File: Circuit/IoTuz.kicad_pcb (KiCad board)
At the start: 2 copper layers, 150 x 95 mm, 93 parts, among them J1 Jack.3.5mm-Mono, P1 ALLIGATOR_01X35, P2 BATTERY, P3 USB_5PIN_SHELL, P4 LED_1, P5 LED_2, P8 IRReceiver, Q1 S8050, Q2 S8050, Q202 FDN340P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

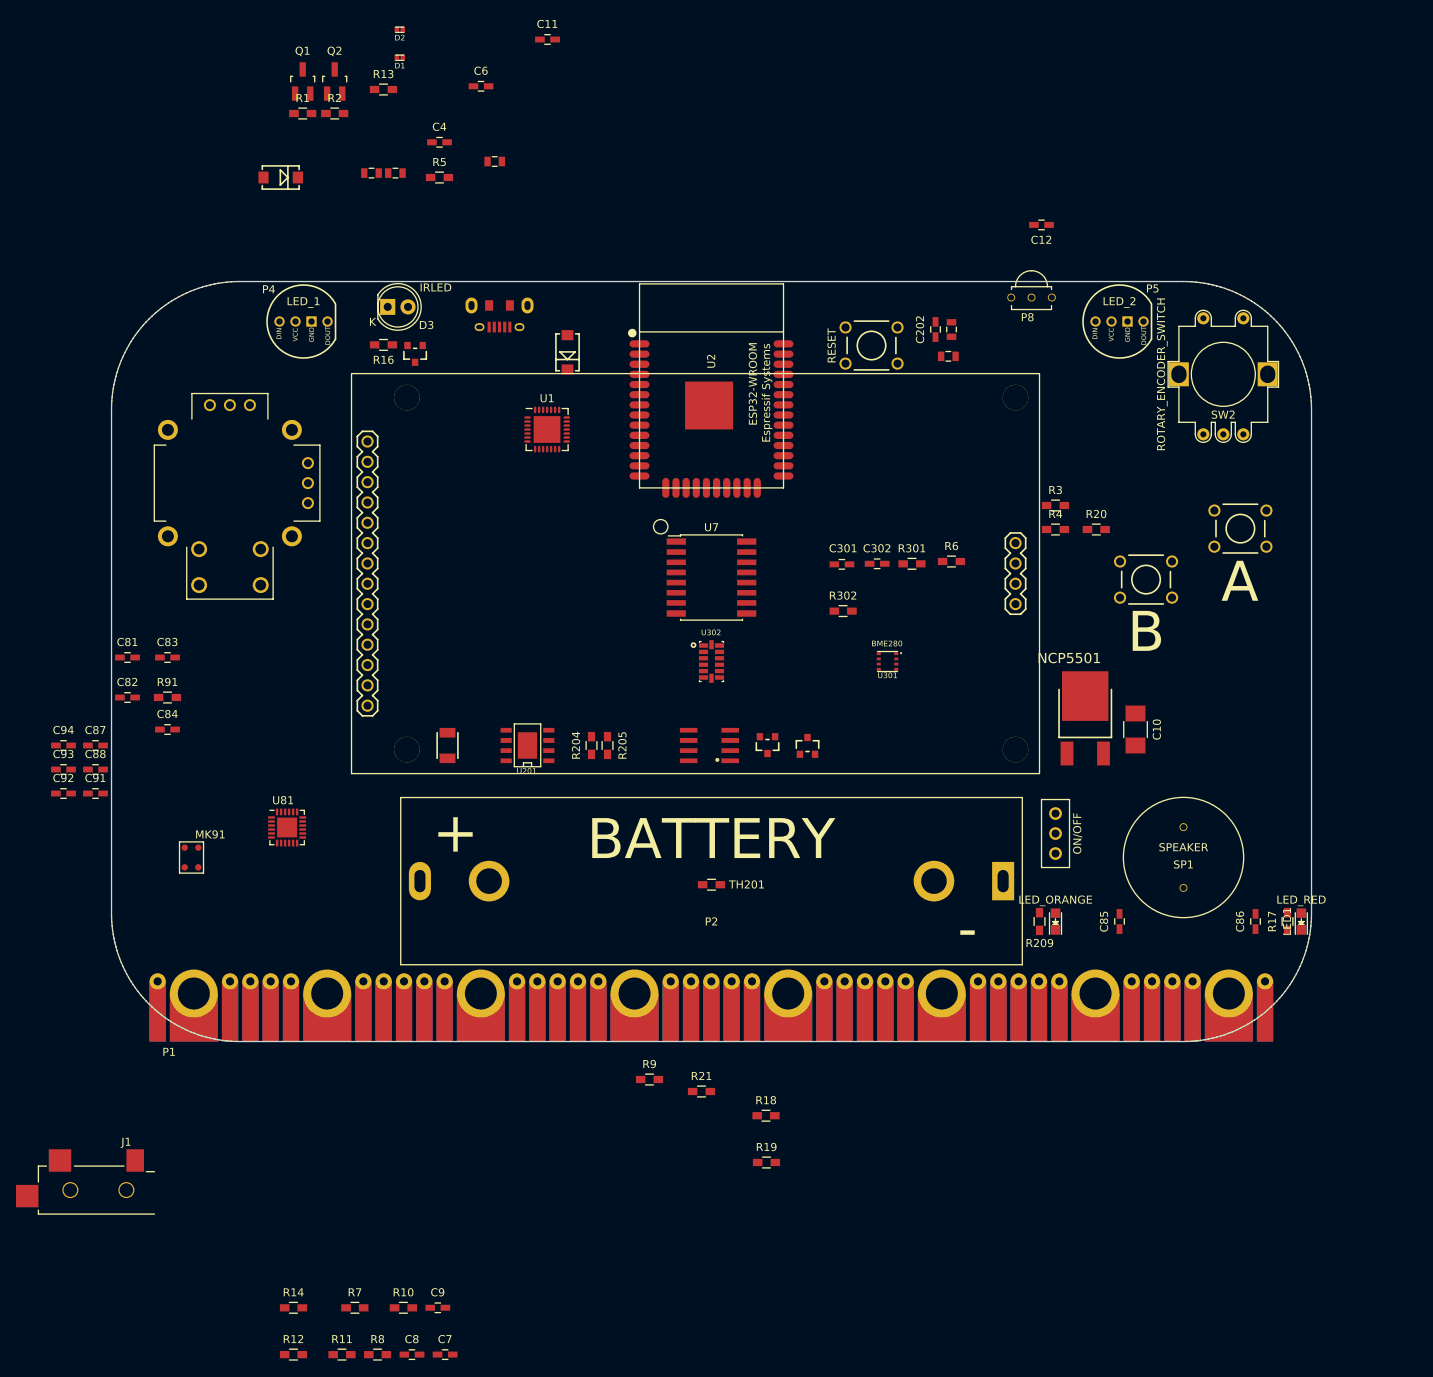
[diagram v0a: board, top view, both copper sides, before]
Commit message: Sectioning nearly complete.
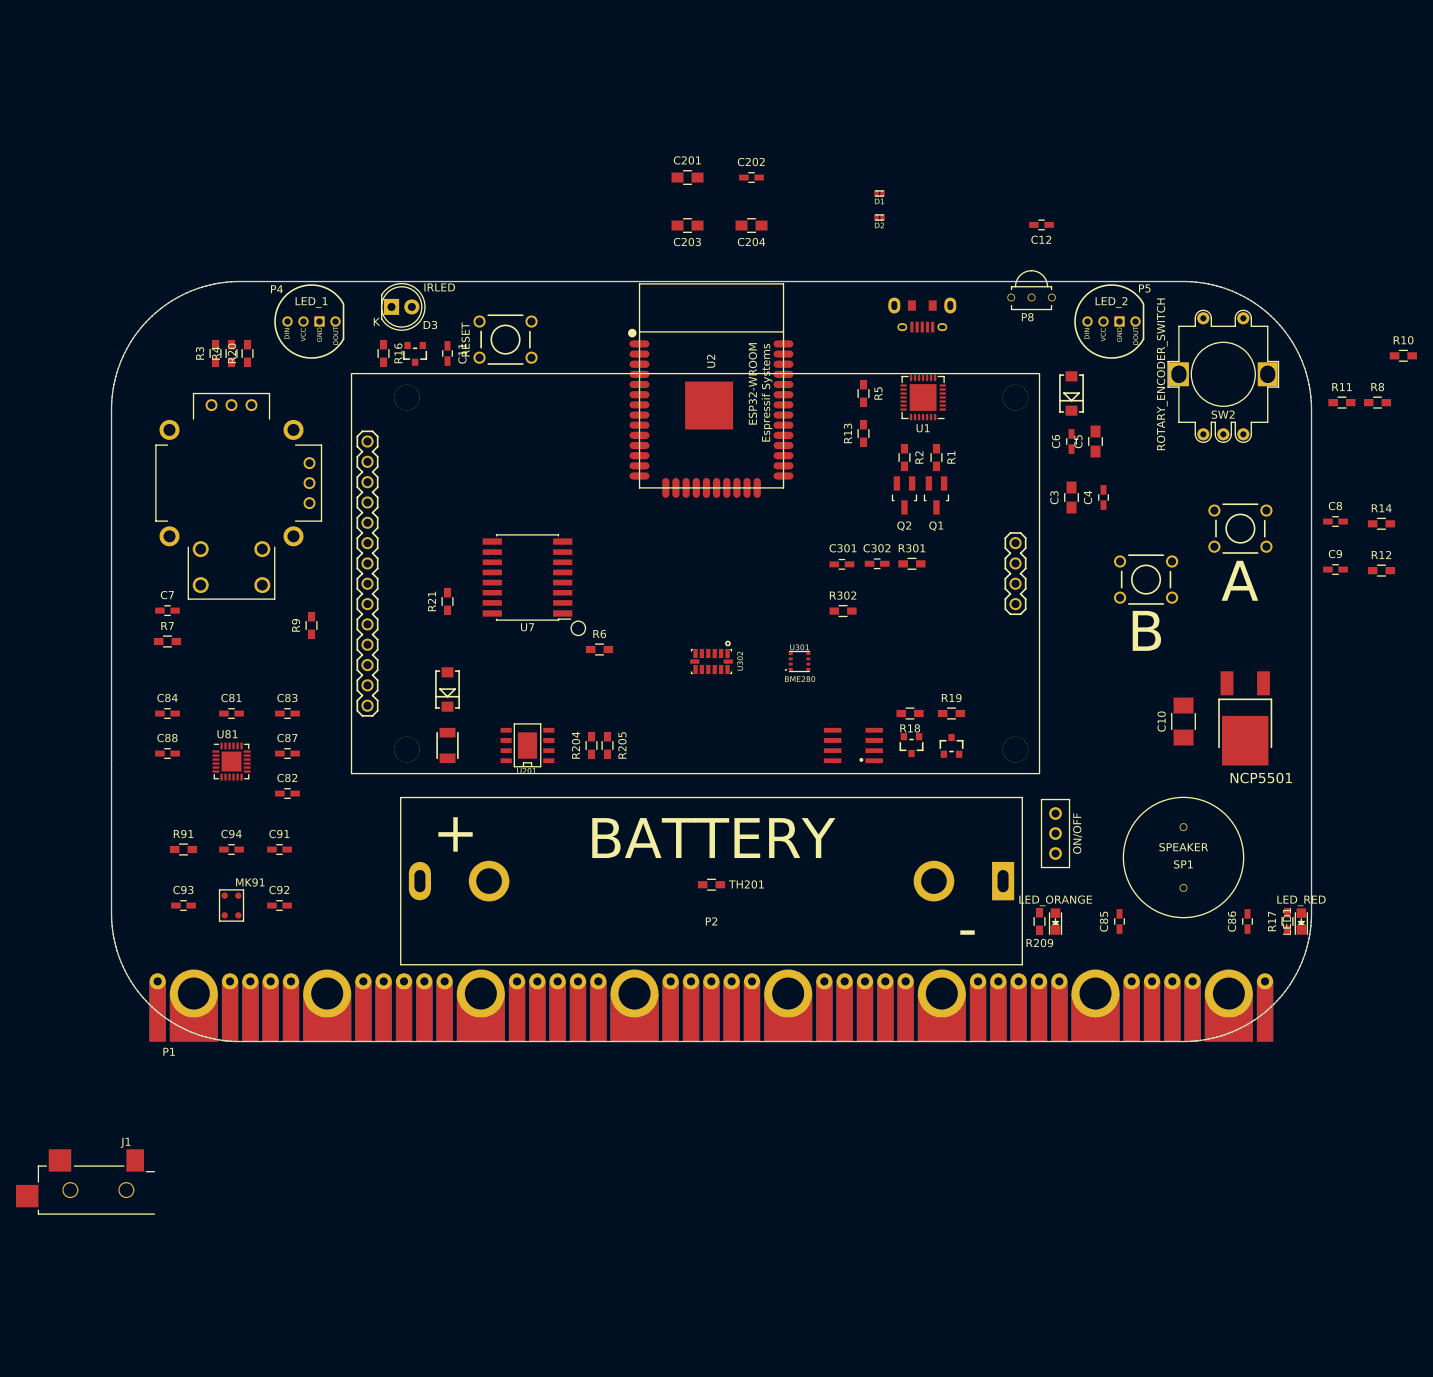
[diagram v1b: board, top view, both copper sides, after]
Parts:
- C201, C203, C204, C3, C5: footprint freetronics_footprints:0805 -> Capacitors_SMD:C_0805_HandSoldering
- moved R10 172.6 mm to (211.5, 64.3)
- moved R11 172.6 mm to (203.8, 70.1)
- moved R8 172.6 mm to (208.3, 70.1)
- moved R12 167.6 mm to (208.7, 91.1)
- moved R14 167.6 mm to (208.7, 85.3)
- moved C8 155.5 mm to (203.0, 85.0)
- moved C9 145.3 mm to (203.0, 91.0)
- moved R20 108.4 mm to (67.0, 64.0), turned to 90 degrees
- moved R3 106.7 mm to (63.0, 64.0), turned to 90 degrees
- moved R4 105.3 mm to (65.0, 64.0), turned to 90 degrees
- moved C7 99.3 mm to (57.0, 96.1)
- moved C5 96.5 mm to (173.0, 75.0), turned to 90 degrees
- moved Q1 94.6 mm to (153.1, 81.7), turned to 180 degrees
- moved C4 94.1 mm to (174.0, 82.0), turned to 90 degrees
- moved C3 93.7 mm to (170.0, 82.0), turned to 90 degrees
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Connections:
- net /ADXL_INT renamed /ACCEL_INT

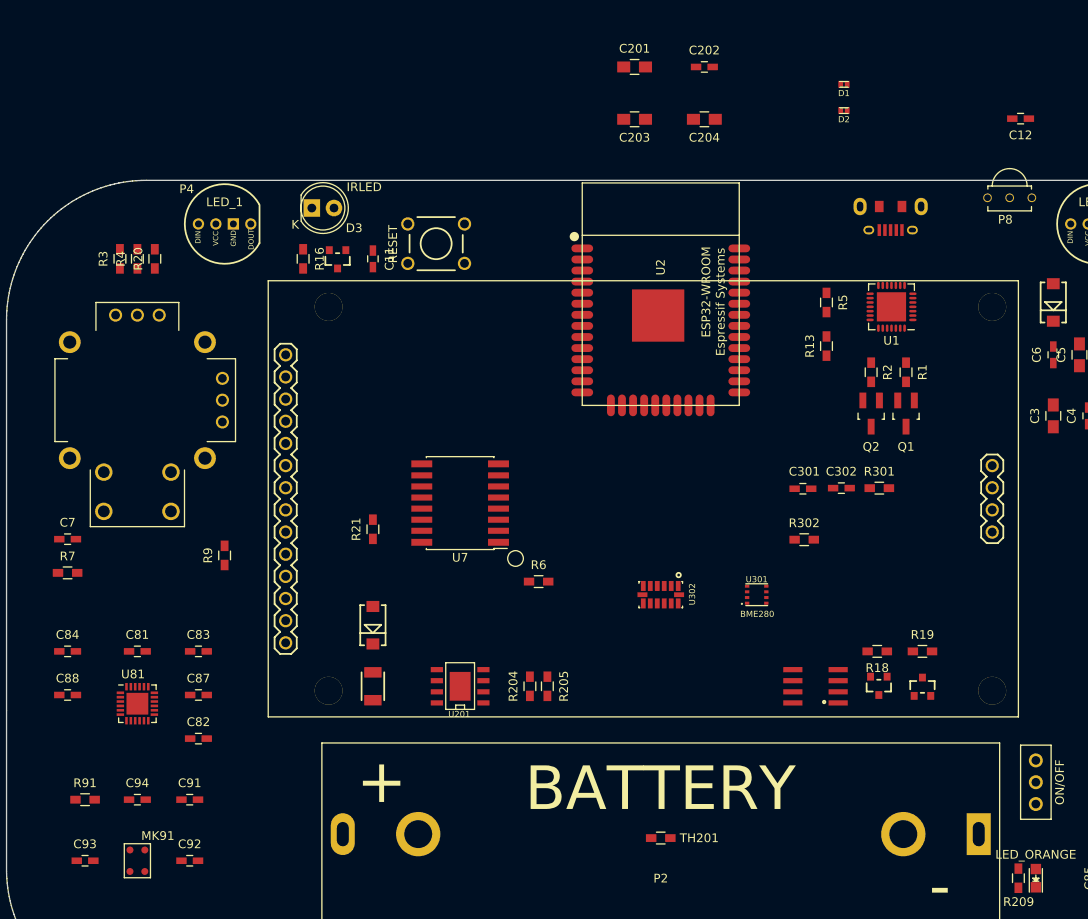
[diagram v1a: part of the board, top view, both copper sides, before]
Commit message: Audio section detail nearly done.
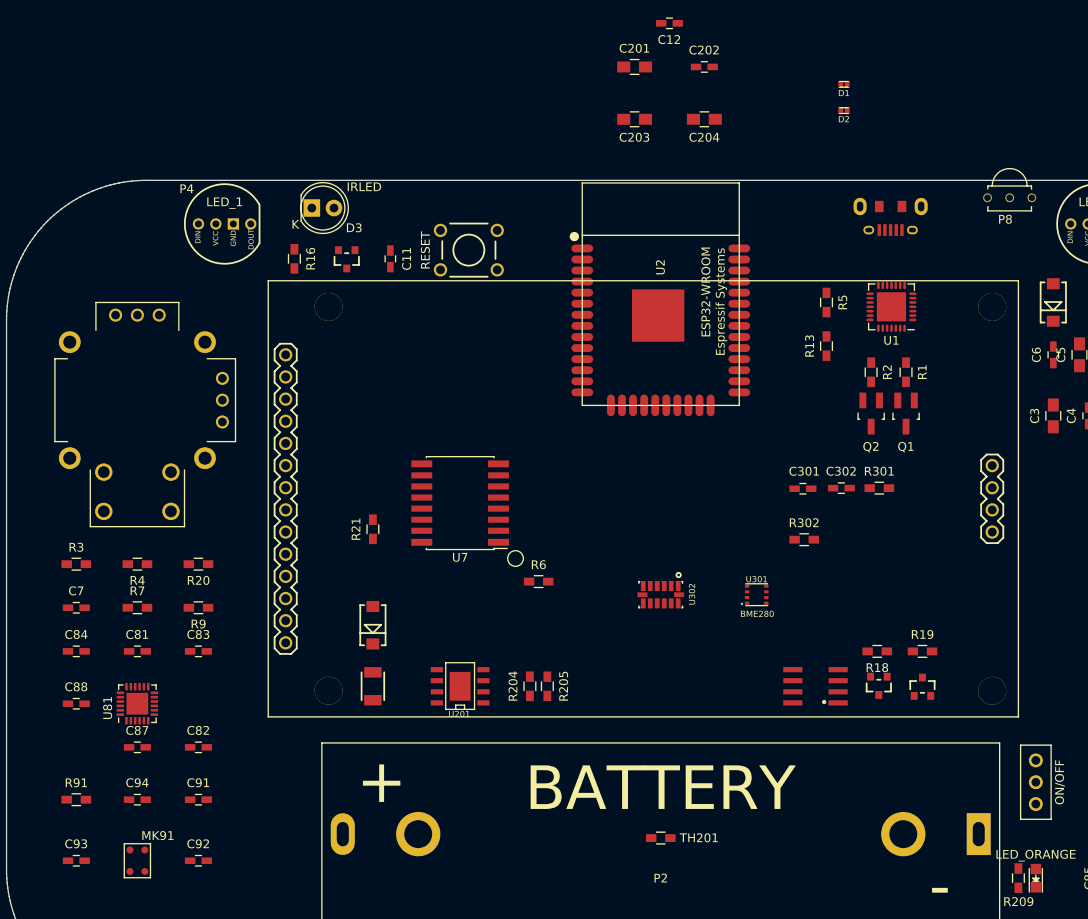
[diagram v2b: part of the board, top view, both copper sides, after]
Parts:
- moved C12 41.7 mm to (126.0, 37.0)
- moved R20 35.4 mm to (72.0, 99.0), turned to 180 degrees
- moved R3 35.4 mm to (58.0, 99.0), turned to 0 degrees
- moved R4 35.0 mm to (65.0, 99.0), turned to 180 degrees
- moved C87 9.22 mm to (65.0, 120.0)
- moved R7 8.94 mm to (65.0, 104.0)
- moved C7 7.93 mm to (58.0, 104.0)
- moved R9 6.71 mm to (72.0, 104.0), turned to 180 degrees
- moved SW5 3.82 mm to (103.0, 63.0)
- moved C11 2.00 mm to (94.0, 64.0)
- moved C88 1.41 mm to (58.0, 115.0)
- moved Q4 1.05 mm to (89.0, 64.0)
- moved C82 1.00 mm to (72.0, 120.0)
- moved C84 1.00 mm to (58.0, 109.0)
- moved C91 1.00 mm to (72.0, 126.0)
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
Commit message: Some recommendations from Angus.
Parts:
- added R15: 10K, Resistors_SMD:R_0603_HandSoldering, F.Cu at (86.0, 64.0)
- C11: value 1nF -> 1uF
- Q4: value MOSFET_N -> FDN340P
- moved J1 142.1 mm to (103.0, 36.0), turned to 90 degrees
- moved R14 39.7 mm to (169.0, 86.0), turned to 270 degrees
- moved R12 36.1 mm to (173.0, 86.0), turned to 90 degrees
- moved R10 30.8 mm to (185.0, 80.0), turned to 270 degrees
- moved R8 29.0 mm to (181.0, 80.0), turned to 270 degrees
- moved R11 28.6 mm to (177.0, 80.0), turned to 90 degrees
- moved C9 26.5 mm to (177.0, 86.0), turned to 90 degrees
- moved R21 20.0 mm to (112.0, 96.0), turned to 180 degrees
- moved C8 18.0 mm to (185.0, 86.0), turned to 90 degrees
- moved R6 13.9 mm to (118.0, 113.0), turned to 270 degrees
- moved U3 8.14 mm to (184.0, 107.0), turned to 270 degrees
- moved D201 8.06 mm to (177.0, 73.0)
- moved U7 6.62 mm to (99.6, 85.8)
- moved C10 5.00 mm to (184.0, 115.0), turned to 180 degrees
- moved U301 4.00 mm to (140.0, 102.5)
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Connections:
- Q4 pad D: +3V3 -> Net-(Q4-PadD)
- Q4 pad S: Net-(Q4-PadS) -> +3V3
- R16 pad 1: Net-(Q4-PadS) -> Net-(Q4-PadD)
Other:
- net class CurrentCarry added: clearance 0.254, trace_width 0.25, via_dia 0.6, via_drill 0.4
- net class Default: clearance 0.2 -> 0.2032; trace_width 0.25 -> 0.2032
- rule trace_clearance: 0.2 -> 0.2032

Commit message: More sectioning. Nearly there.
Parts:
- added Q3: FDN340P, freetronics_footprints:SOT23_FET, F.Cu at (93.0, 95.0)
- added R22: 10K, Resistors_SMD:R_0603_HandSoldering, F.Cu at (96.0, 95.0)
- moved C12 86.4 mm to (184.0, 101.0), turned to 0 degrees
- moved C204 74.8 mm to (93.0, 113.0), turned to 270 degrees
- moved C201 71.1 mm to (118.0, 113.0), turned to 270 degrees
- moved R301 50.3 mm to (100.0, 95.0), turned to 90 degrees
- moved C302 47.9 mm to (98.0, 95.0), turned to 270 degrees
- moved R302 39.5 mm to (102.0, 95.0), turned to 90 degrees
- moved C301 37.6 mm to (104.0, 95.0), turned to 270 degrees
- moved C202 27.8 mm to (113.0, 64.0), turned to 90 degrees
- moved C203 20.0 mm to (110.0, 64.0), turned to 90 degrees
- moved D1 19.4 mm to (150.0, 63.0)
- moved D2 17.5 mm to (153.0, 63.0), turned to 180 degrees
- moved R204 10.0 mm to (120.0, 113.0)
- moved R205 9.00 mm to (122.0, 113.0)
- moved D4 8.06 mm to (96.0, 113.0)
- moved F1 8.00 mm to (100.0, 113.0)
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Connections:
- U6 pad 8: /BL_Control -> Net-(Q3-PadD)
- U7 pad 10: /BL_Control -> /Touch_INT
- U7 pad 12: /SD_Sel -> /BL_Control
- U7 pad 7: /Touch_INT -> /SD_Sel

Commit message: Pushing things around.
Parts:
- moved D201 65.6 mm to (125.0, 113.0)
- moved C5 60.2 mm to (128.0, 113.0)
- moved R6 24.1 mm to (108.0, 97.0)
- moved R14 11.2 mm to (171.0, 75.0)
- moved C6 10.8 mm to (159.0, 69.0)
- moved C3 10.2 mm to (171.0, 70.0)
- moved C4 10.2 mm to (175.0, 70.0)
- moved R11 10.2 mm to (179.0, 70.0)
- moved C8 8.49 mm to (179.0, 80.0)
- moved C9 8.49 mm to (171.0, 80.0), turned to 270 degrees
- moved R10 7.81 mm to (179.0, 75.0)
- moved R8 7.81 mm to (175.0, 75.0)
- moved R12 6.32 mm to (175.0, 80.0)
- moved C202 3.00 mm to (110.0, 64.0)
- moved C203 3.00 mm to (107.0, 64.0)
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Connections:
- net Net-(C85-Pad1) renamed /Audio/Speaker-
- net Net-(C86-Pad1) renamed /Audio/Speaker+

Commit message: Some important traces and shoving components about.
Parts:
- removed J1: Jack.3.5mm-Mono, libs:3.5mmMonoTSJack.MJ-3523-SMT.Switch
- moved C93 28.7 mm to (72.0, 108.0)
- moved MK91 25.0 mm to (65.0, 108.0)
- moved C92 23.6 mm to (58.0, 114.0)
- moved LED201 22.2 mm to (172.0, 113.0)
- moved R209 22.2 mm to (169.0, 113.0)
- moved LED1 22.0 mm to (198.7, 113.0)
- moved R17 22.0 mm to (196.0, 113.0)
- moved C83 21.3 mm to (58.0, 125.0), turned to 180 degrees
- moved R91 18.0 mm to (58.0, 108.0), turned to 180 degrees
- moved C81 17.5 mm to (72.0, 125.0)
- moved C88 14.6 mm to (72.0, 119.0), turned to 180 degrees
- moved C91 13.9 mm to (65.0, 114.0), turned to 180 degrees
- moved C94 13.9 mm to (72.0, 114.0)
- moved C87 12.2 mm to (72.0, 130.0), turned to 180 degrees
- moved C84 10.0 mm to (58.0, 119.0), turned to 180 degrees
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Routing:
- net /Audio/Speaker+: track 0.00 -> 137.4 mm
- net /Audio/Speaker-: track 0.00 -> 131.4 mm
- net +3V3: track 0.00 -> 21.3 mm
- net /Audio/MIC-: track 0.00 -> 13.3 mm
- net Net-(C93-Pad1): track 0.00 -> 11.9 mm
- net GND: track 0.00 -> 2.05 mm
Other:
- net class 12mil added: clearance 0.254, trace_width 0.3048, via_dia 0.6, via_drill 0.4
- net class CurrentCarry: clearance 0.254 -> 0.2032
- rule trace_min: 0.2 -> 0.1524
